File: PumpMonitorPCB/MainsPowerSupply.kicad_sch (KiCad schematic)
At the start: 30 parts, among them K1 J115F11CH5VDCS61-5U, Q1 AS2302, U1 ACS770xCB-050B-PFF, U2 AMS1117-3.3, U3 LMV321, U4 LMV321

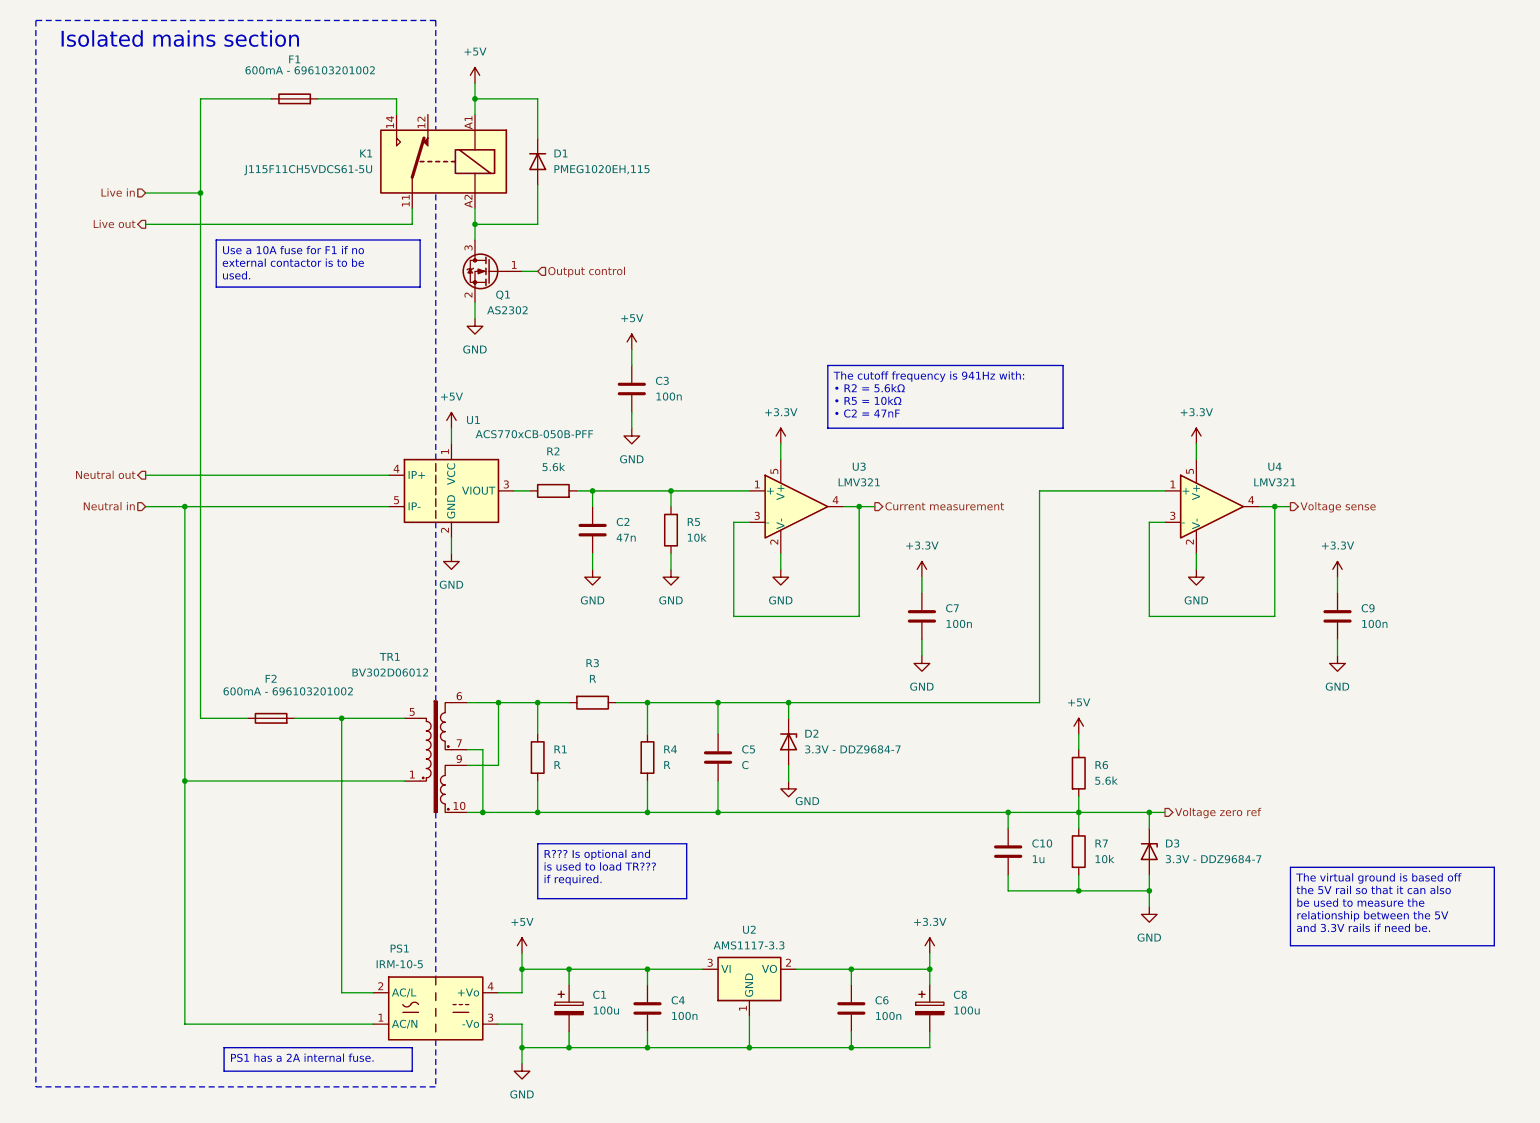
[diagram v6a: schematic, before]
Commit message: Added terminals footprint and 3D model.
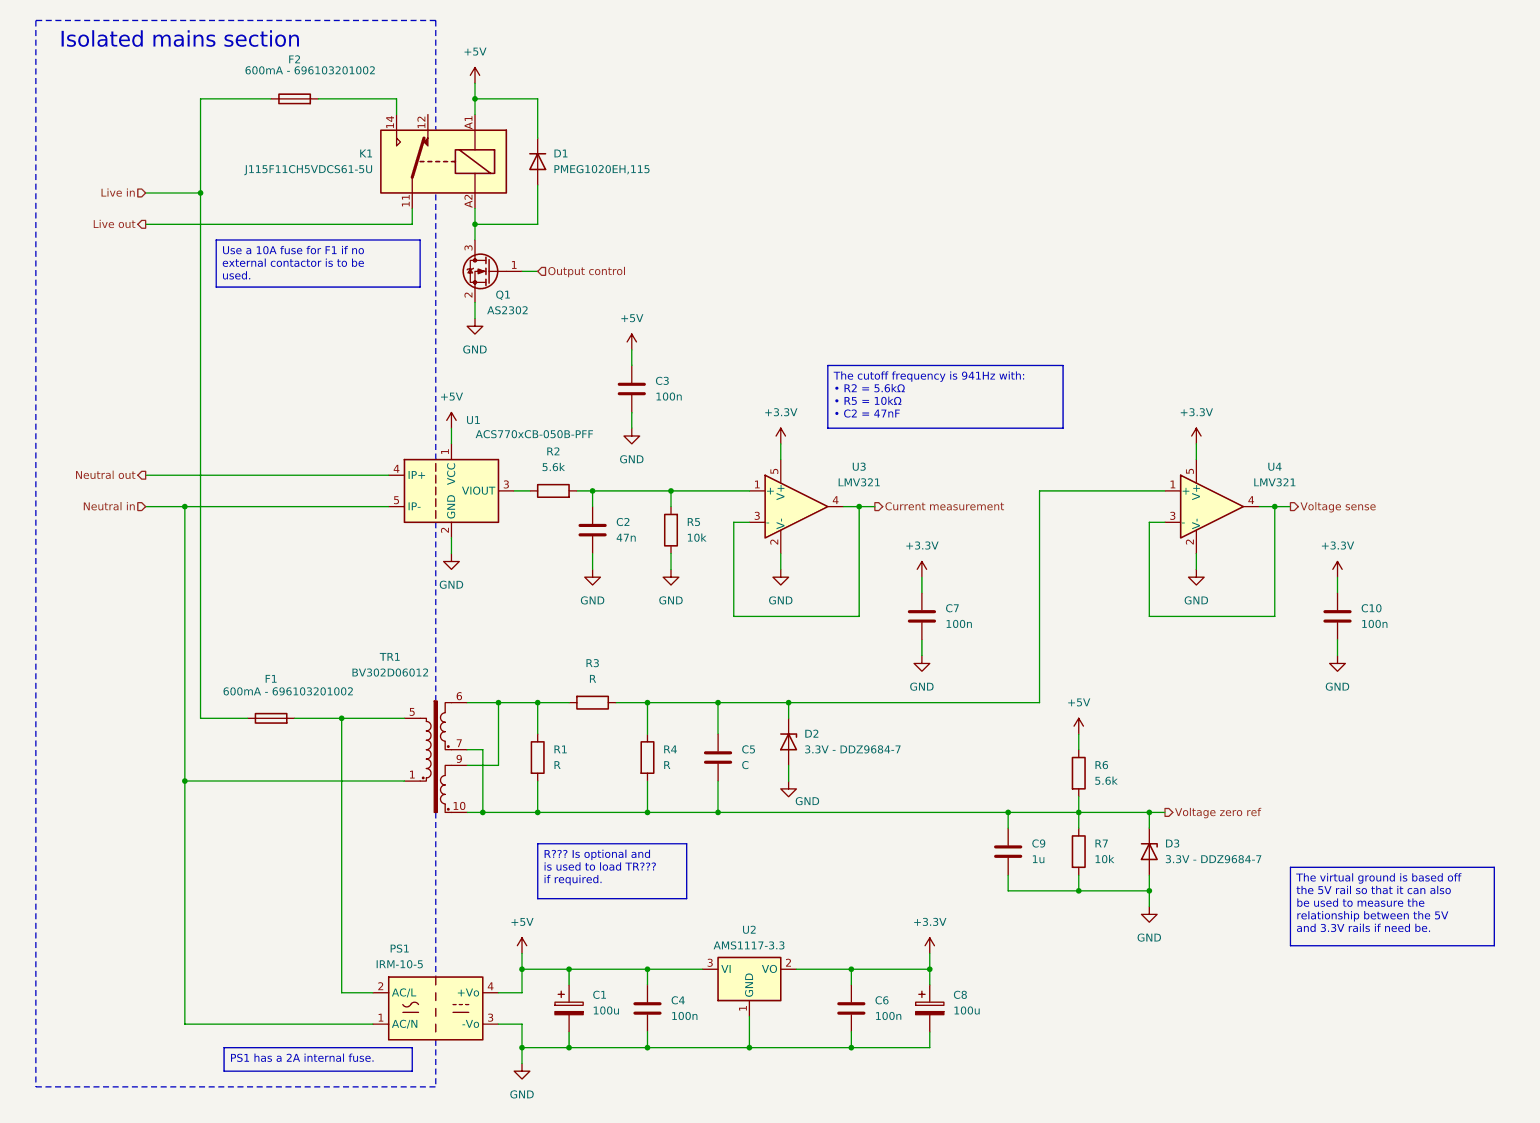
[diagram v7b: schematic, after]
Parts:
- TR1: footprint (none) -> PumpMonitorCustomFootprints:Transformer_BV302D06012
- renumbered C9 to C10, C10 to C9, F2 to F1, F1 to F2
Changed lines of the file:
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@@
 		(on_board yes)
 		(dnp no)
-		(property "Reference" "F2"
+		(property "Reference" "F1"
 			(at 52.07 120.65 90)
 			(effects
@@
 			(project "PumpMonitorPCB"
 				(path "/c90c4964-ca1b-44d9-8ea9-8989903af0f2/519408a1-89cc-4bd2-9b7b-cb03d2ff4d33/d43e5729-96b5-4892-980a-41f5073f0d0e"
-					(reference "F2")
+					(reference "F1")
 					(unit 1)
 				)
@@
 		(dnp no)
 		(fields_autoplaced yes)
-		(property "Reference" "#PWR020"
+		(property "Reference" "#PWR022"
 			(at 224.79 107.95 0)
 			(effects
@@
 			(project "PumpMonitorPCB"
 				(path "/c90c4964-ca1b-44d9-8ea9-8989903af0f2/519408a1-89cc-4bd2-9b7b-cb03d2ff4d33/d43e5729-96b5-4892-980a-41f5073f0d0e"
-					(reference "#PWR020")
+					(reference "#PWR022")
 					(unit 1)
 				)
@@
 		(pin "1"
 		)
+		(instances
+			(project "PumpMonitorPCB"
+				(path "/c90c4964-ca1b-44d9-8ea9-8989903af0f2/519408a1-89cc-4bd2-9b7b-cb03d2ff4d33/d43e5729-96b5-4892-980a-41f5073f0d0e"
+					(reference "R7")
+					(unit 1)
+				)
+			)
+		)
 	)
 	(symbol
@@
 		(dnp no)
 		(fields_autoplaced yes)
-		(property "Reference" "#PWR021"
+		(property "Reference" "#PWR023"
 			(at 224.79 123.19 0)
 			(effects
@@
 			(project "PumpMonitorPCB"
 				(path "/c90c4964-ca1b-44d9-8ea9-8989903af0f2/519408a1-89cc-4bd2-9b7b-cb03d2ff4d33/d43e5729-96b5-4892-980a-41f5073f0d0e"
-					(reference "#PWR021")
+					(reference "#PWR023")
 					(unit 1)
 				)
@@
 		(dnp no)
 		(fields_autoplaced yes)
-		(property "Reference" "#PWR022"
+		(property "Reference" "#PWR018"
 			(at 182.88 133.35 0)
 			(effects
@@
 			(project "PumpMonitorPCB"
 				(path "/c90c4964-ca1b-44d9-8ea9-8989903af0f2/519408a1-89cc-4bd2-9b7b-cb03d2ff4d33/d43e5729-96b5-4892-980a-41f5073f0d0e"
-					(reference "#PWR022")
+					(reference "#PWR018")
 					(unit 1)
 				)
@@
 			)
 		)
-		(property "Footprint" ""
+		(property "Footprint" "PumpMonitorCustomFootprints:Transformer_BV302D06012"
 			(at 78.74 146.05 0)
 			(effects
@@
 		(pin "6"
 		)
+		(instances
+			(project "PumpMonitorPCB"
+				(path "/c90c4964-ca1b-44d9-8ea9-8989903af0f2/519408a1-89cc-4bd2-9b7b-cb03d2ff4d33/d43e5729-96b5-4892-980a-41f5073f0d0e"
+					(reference "TR1")
+					(unit 1)
+				)
+			)
+		)
 	)
 	(symbol
@@
 		(dnp no)
 		(fields_autoplaced yes)
-		(property "Reference" "#PWR019"
+		(property "Reference" "#PWR017"
 			(at 158.75 168.91 0)
 			(effects
@@
 			(project "PumpMonitorPCB"
 				(path "/c90c4964-ca1b-44d9-8ea9-8989903af0f2/519408a1-89cc-4bd2-9b7b-cb03d2ff4d33/d43e5729-96b5-4892-980a-41f5073f0d0e"
-					(reference "#PWR019")
+					(reference "#PWR017")
 					(unit 1)
 				)
@@
 		(on_board yes)
 		(dnp no)
-		(property "Reference" "C10"
+		(property "Reference" "C9"
 			(at 175.26 147.3199 0)
 			(effects
@@
 		(pin "2"
 		)
+		(instances
+			(project "PumpMonitorPCB"
+				(path "/c90c4964-ca1b-44d9-8ea9-8989903af0f2/519408a1-89cc-4bd2-9b7b-cb03d2ff4d33/d43e5729-96b5-4892-980a-41f5073f0d0e"
+					(reference "C9")
+					(unit 1)
+				)
+			)
+		)
 	)
 	(symbol
@@
 		(on_board yes)
 		(dnp no)
-		(property "Reference" "F1"
+		(property "Reference" "F2"
 			(at 55.88 20.32 90)
 			(effects
@@
 			(project "PumpMonitorPCB"
 				(path "/c90c4964-ca1b-44d9-8ea9-8989903af0f2/519408a1-89cc-4bd2-9b7b-cb03d2ff4d33/d43e5729-96b5-4892-980a-41f5073f0d0e"
-					(reference "F1")
+					(reference "F2")
 					(unit 1)
 				)
@@
 		(pin "2"
 		)
+		(instances
+			(project "PumpMonitorPCB"
+				(path "/c90c4964-ca1b-44d9-8ea9-8989903af0f2/519408a1-89cc-4bd2-9b7b-cb03d2ff4d33/d43e5729-96b5-4892-980a-41f5073f0d0e"
+					(reference "D3")
+					(unit 1)
+				)
+			)
+		)
 	)
 	(symbol
@@
 		(dnp no)
 		(fields_autoplaced yes)
-		(property "Reference" "#PWR015"
+		(property "Reference" "#PWR020"
 			(at 201.93 86.36 0)
 			(effects
@@
 			(project "PumpMonitorPCB"
 				(path "/c90c4964-ca1b-44d9-8ea9-8989903af0f2/519408a1-89cc-4bd2-9b7b-cb03d2ff4d33/d43e5729-96b5-4892-980a-41f5073f0d0e"
-					(reference "#PWR015")
+					(reference "#PWR020")
 					(unit 1)
 				)
@@
 		(dnp no)
 		(fields_autoplaced yes)
-		(property "Reference" "#PWR023"
+		(property "Reference" "#PWR019"
 			(at 194.31 163.83 0)
 			(effects
@@
 			(project "PumpMonitorPCB"
 				(path "/c90c4964-ca1b-44d9-8ea9-8989903af0f2/519408a1-89cc-4bd2-9b7b-cb03d2ff4d33/d43e5729-96b5-4892-980a-41f5073f0d0e"
-					(reference "#PWR023")
+					(reference "#PWR019")
 					(unit 1)
 				)
@@
 		(pin "2"
 		)
+		(instances
+			(project "PumpMonitorPCB"
+				(path "/c90c4964-ca1b-44d9-8ea9-8989903af0f2/519408a1-89cc-4bd2-9b7b-cb03d2ff4d33/d43e5729-96b5-4892-980a-41f5073f0d0e"
+					(reference "R6")
+					(unit 1)
+				)
+			)
+		)
 	)
 	(symbol
@@
 		(dnp no)
 		(fields_autoplaced yes)
-		(property "Reference" "#PWR017"
+		(property "Reference" "#PWR015"
 			(at 157.48 107.95 0)
 			(effects
@@
 			(project "PumpMonitorPCB"
 				(path "/c90c4964-ca1b-44d9-8ea9-8989903af0f2/519408a1-89cc-4bd2-9b7b-cb03d2ff4d33/d43e5729-96b5-4892-980a-41f5073f0d0e"
-					(reference "#PWR017")
+					(reference "#PWR015")
 					(unit 1)
 				)
@@
 		(pin "1"
 		)
+		(instances
+			(project "PumpMonitorPCB"
+				(path "/c90c4964-ca1b-44d9-8ea9-8989903af0f2/519408a1-89cc-4bd2-9b7b-cb03d2ff4d33/d43e5729-96b5-4892-980a-41f5073f0d0e"
+					(reference "R3")
+					(unit 1)
+				)
+			)
+		)
 	)
 	(symbol
@@
 		(dnp no)
 		(fields_autoplaced yes)
-		(property "Reference" "#PWR016"
+		(property "Reference" "#PWR021"
 			(at 201.93 109.22 0)
 			(effects
@@
 			(project "PumpMonitorPCB"
 				(path "/c90c4964-ca1b-44d9-8ea9-8989903af0f2/519408a1-89cc-4bd2-9b7b-cb03d2ff4d33/d43e5729-96b5-4892-980a-41f5073f0d0e"
-					(reference "#PWR016")
+					(reference "#PWR021")
 					(unit 1)
 				)
@@
 		(pin "5"
 		)
+		(instances
+			(project "PumpMonitorPCB"
+				(path "/c90c4964-ca1b-44d9-8ea9-8989903af0f2/519408a1-89cc-4bd2-9b7b-cb03d2ff4d33/d43e5729-96b5-4892-980a-41f5073f0d0e"
+					(reference "U3")
+					(unit 1)
+				)
+			)
+		)
 	)
 	(symbol
@@
 		(pin "1"
 		)
+		(instances
+			(project "PumpMonitorPCB"
+				(path "/c90c4964-ca1b-44d9-8ea9-8989903af0f2/519408a1-89cc-4bd2-9b7b-cb03d2ff4d33/d43e5729-96b5-4892-980a-41f5073f0d0e"
+					(reference "R4")
+					(unit 1)
+				)
+			)
+		)
 	)
 	(symbol
@@
 		(dnp no)
 		(fields_autoplaced yes)
-		(property "Reference" "#PWR018"
+		(property "Reference" "#PWR016"
 			(at 157.48 123.19 0)
 			(effects
@@
 			(project "PumpMonitorPCB"
 				(path "/c90c4964-ca1b-44d9-8ea9-8989903af0f2/519408a1-89cc-4bd2-9b7b-cb03d2ff4d33/d43e5729-96b5-4892-980a-41f5073f0d0e"
-					(reference "#PWR018")
+					(reference "#PWR016")
 					(unit 1)
 				)
@@
 		(dnp no)
 		(fields_autoplaced yes)
-		(property "Reference" "C9"
+		(property "Reference" "C10"
 			(at 228.6 109.2199 0)
 			(effects
@@
 			(project "PumpMonitorPCB"
 				(path "/c90c4964-ca1b-44d9-8ea9-8989903af0f2/519408a1-89cc-4bd2-9b7b-cb03d2ff4d33/d43e5729-96b5-4892-980a-41f5073f0d0e"
-					(reference "C9")
+					(reference "C10")
 					(unit 1)
 				)

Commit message: Rejigged auxilliary connectors, experimetning with kiclearance.
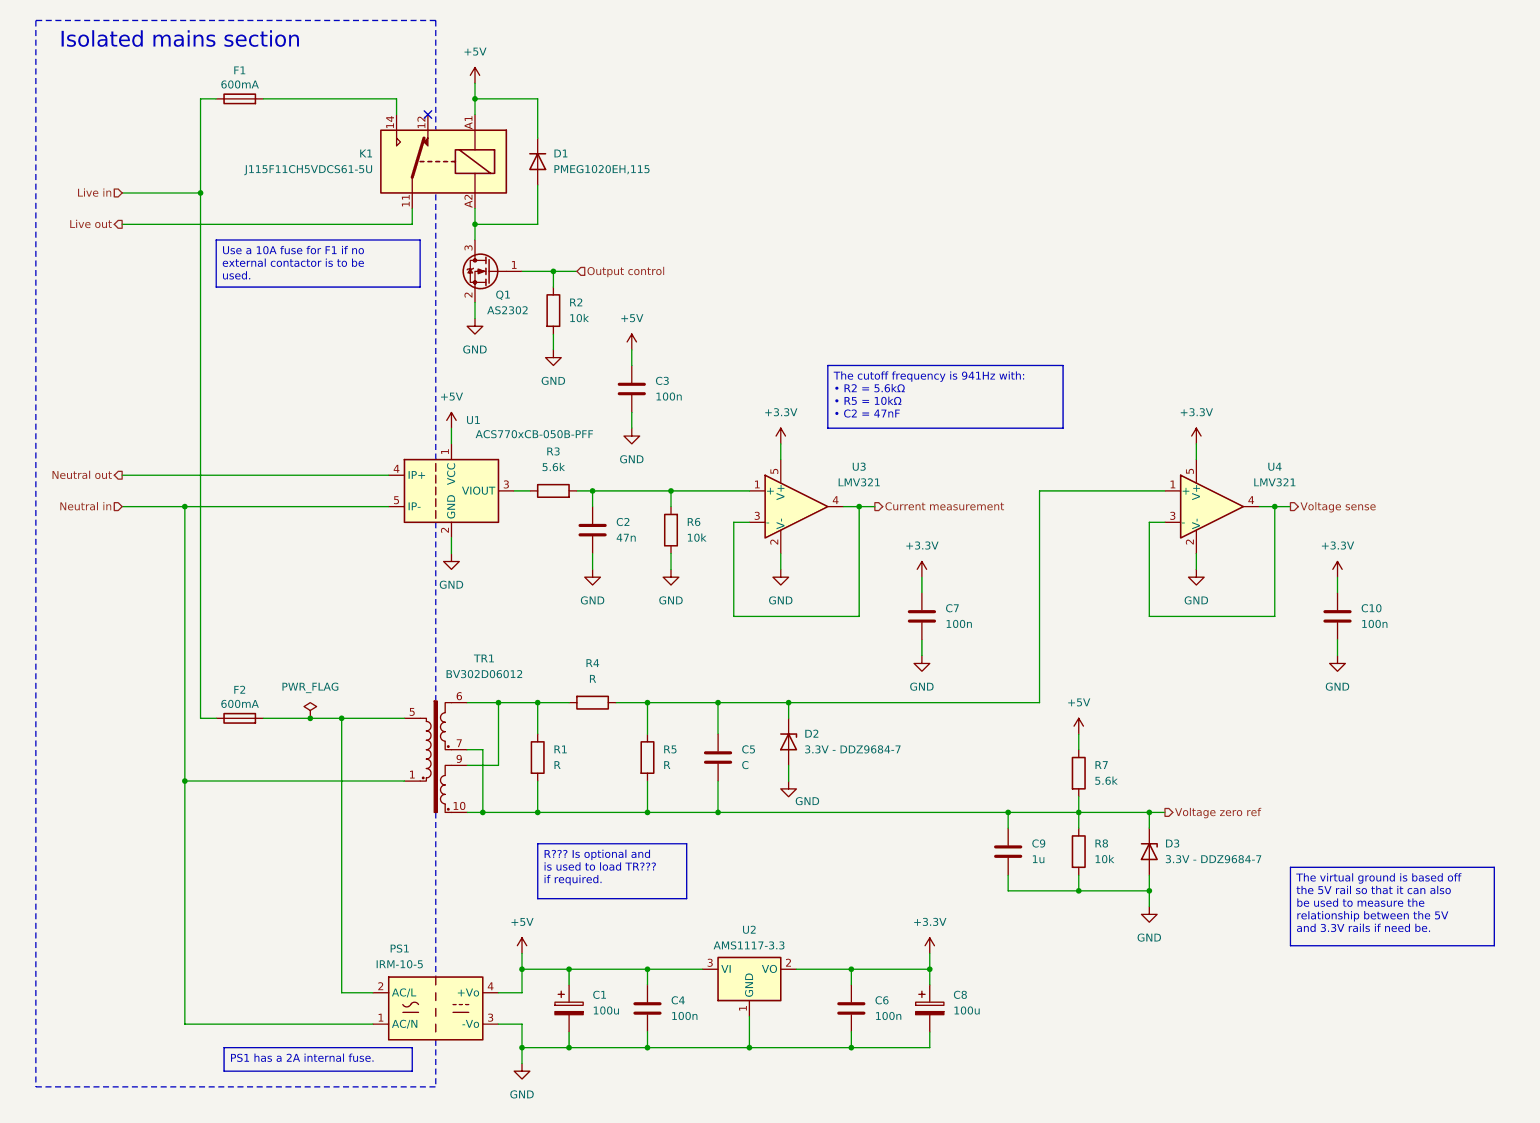
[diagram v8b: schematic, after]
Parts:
- added R2: 10k, Resistor_SMD:R_0603_1608Metric_Pad0.98x0.95mm_HandSolder, symbol Device:R
- C10, C2, C3, C4, C5, C6, C7, C9: footprint Capacitor_SMD:C_0805_2012Metric_Pad1.18x1.45mm_HandSolder -> Capacitor_SMD:C_0603_1608Metric_Pad1.08x0.95mm_HandSolder
- F1: renamed from F2; value 600mA - 696103201002 -> 600mA; Part number (none) -> 696103201002
- F2: renamed from F1; value 600mA - 696103201002 -> 600mA; Part number (none) -> 696103201002
- Q1: PlaceOnSecondary Yes -> (none)
- R1: footprint Resistor_THT:R_Axial_DIN0207_L6.3mm_D2.5mm_P7.62mm_Horizontal -> Resistor_THT:R_Axial_DIN0309_L9.0mm_D3.2mm_P12.70mm_Horizontal
- R3: renamed from R2; footprint Resistor_SMD:R_0805_2012Metric_Pad1.20x1.40mm_HandSolder -> Resistor_SMD:R_0603_1608Metric_Pad0.98x0.95mm_HandSolder
- R4: renamed from R3; footprint Resistor_SMD:R_0805_2012Metric_Pad1.20x1.40mm_HandSolder -> Resistor_SMD:R_0603_1608Metric_Pad0.98x0.95mm_HandSolder
- R5: renamed from R4; footprint Resistor_SMD:R_0805_2012Metric_Pad1.20x1.40mm_HandSolder -> Resistor_SMD:R_0603_1608Metric_Pad0.98x0.95mm_HandSolder
- R6: renamed from R5; footprint Resistor_SMD:R_0805_2012Metric_Pad1.20x1.40mm_HandSolder -> Resistor_SMD:R_0603_1608Metric_Pad0.98x0.95mm_HandSolder
- R7: renamed from R6; footprint Resistor_SMD:R_0805_2012Metric_Pad1.20x1.40mm_HandSolder -> Resistor_SMD:R_0603_1608Metric_Pad0.98x0.95mm_HandSolder
- R8: renamed from R7; footprint Resistor_SMD:R_0805_2012Metric_Pad1.20x1.40mm_HandSolder -> Resistor_SMD:R_0603_1608Metric_Pad0.98x0.95mm_HandSolder
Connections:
- net GND: now also R2.2
- net Output control: now also R2.1
- no-connect marks 0 -> 1
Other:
- moved on the sheet: F1, F2
